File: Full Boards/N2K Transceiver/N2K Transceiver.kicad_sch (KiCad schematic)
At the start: 67 parts, among them J1 PSU TP, J3 Optional Bond, SW1 SW_MEC_5G, SW2 SW_MEC_5G, SW3 SW_MEC_5G

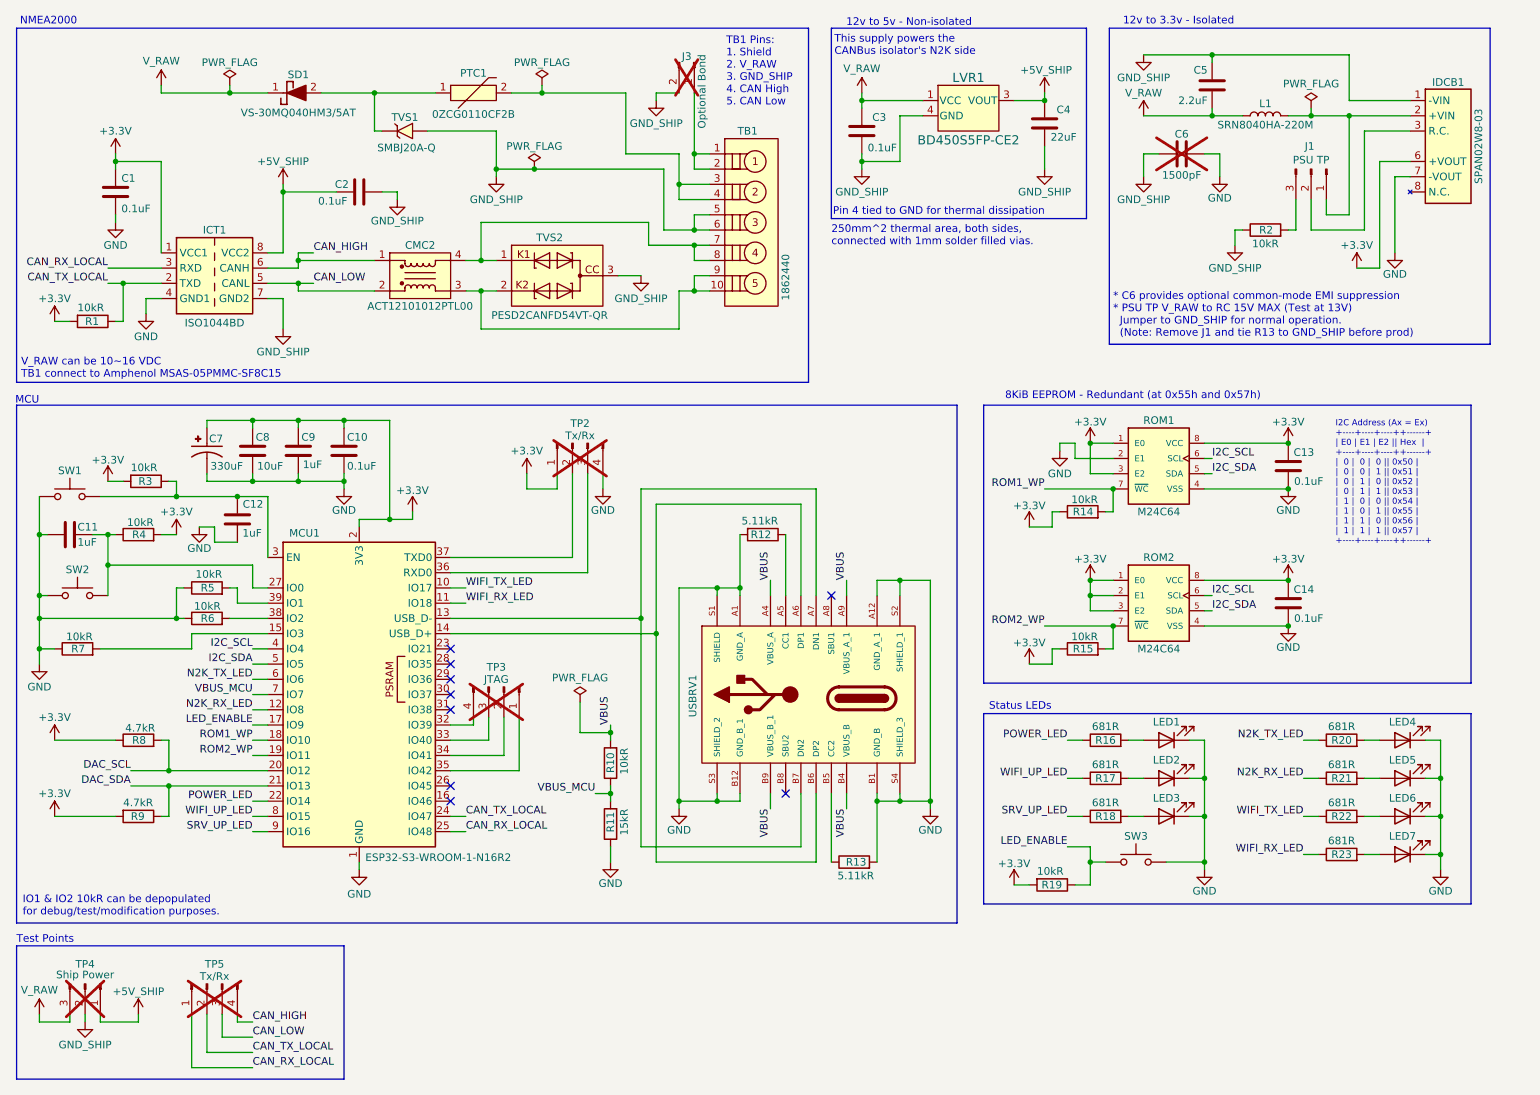
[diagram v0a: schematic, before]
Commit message: Added pull-ups to the I2C SDA/SCL pins. Removed old DAC pull-ups and nets. Added a space between the CAN-H/L and Tx/Rx test points for isolation.
Signed-off-by: digimer <digital.mermaid@gmail.com>
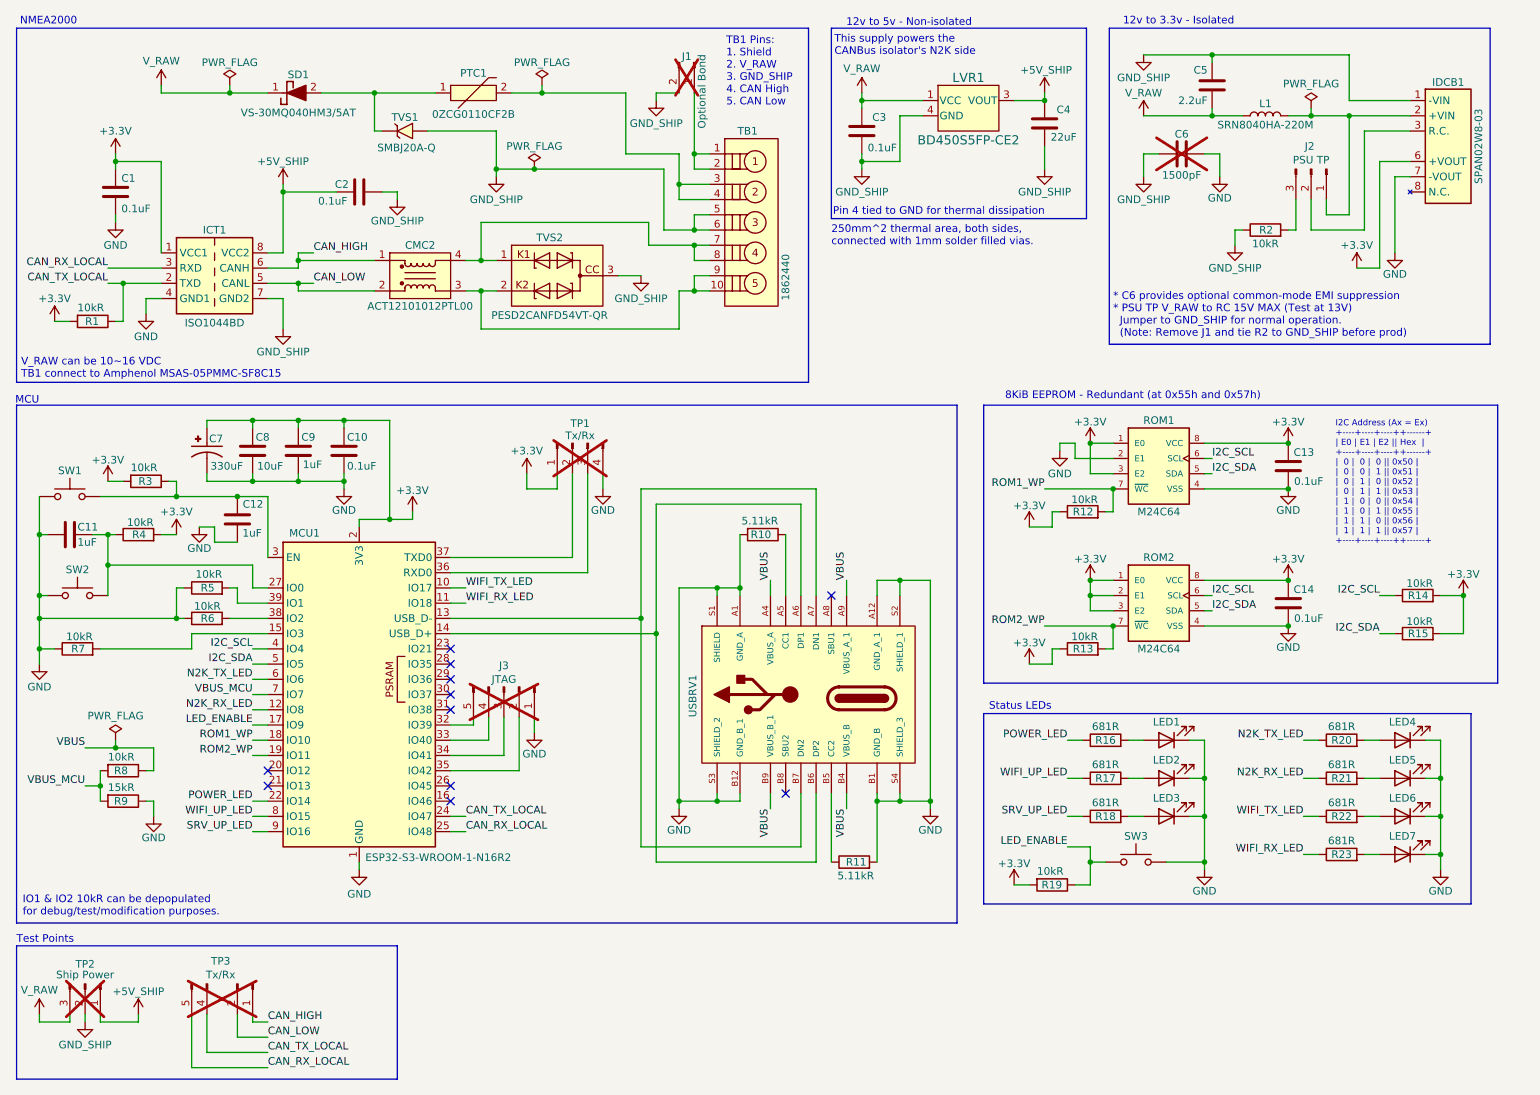
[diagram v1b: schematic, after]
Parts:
- removed R8, R9: 4.7kR, mr-stuff:Stackpole_RNCP1206, symbol Device:R
- removed TP5: Tx/Rx, Connector_PinHeader_2.54mm:PinHeader_1x04_P2.54mm_Vertical, symbol Connector:Conn_01x04_Pin
- added R14, R15: 10kR, mr-stuff:Stackpole_RNCP1206, symbol Device:R
- added TP3: Tx/Rx, symbol mr-parts:Conn_01x05_Pin_No_Pin_3
- J3: renamed from TP3; footprint Connector_PinHeader_2.54mm:PinHeader_1x04_P2.54mm_Vertical -> Connector_PinHeader_2.54mm:PinHeader_1x05_P2.54mm_Vertical; symbol Connector:Conn_01x04_Pin -> Connector:Conn_01x05_Pin; Part Amphenol 68001-416HLF -> (none); now in the parts list
- renumbered J3 to J1, J1 to J2, R12 to R10, R13 to R11, R14 to R12, R15 to R13, R10 to R8, R11 to R9, TP2 to TP1, TP4 to TP2
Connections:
- net +3.3V: now also R14.2, R15.2
- net CAN_HIGH: now also TP3.1 (Pin_1)
- net CAN_LOW: now also TP3.2 (Pin_2)
- net CAN_RX_LOCAL: now also TP3.5 (Pin_5)
- net CAN_TX_LOCAL: now also TP3.4 (Pin_4)
- net GND: now also J3.1 (Pin_1)
- net I2C_SCL: now also R14.1
- net I2C_SDA: now also R15.1
- net VBUS: now also R8.1; no longer R8.2
- net VBUS_MCU: now also R8.2; no longer R8.1
- net at MCU1.35 (IO42): now also J3.2 (Pin_2); no longer J3.1 (Pin_1)
- net at MCU1.34 (IO41): now also J3.3 (Pin_3); no longer J3.2 (Pin_2)
- net at MCU1.33 (IO40): now also J3.4 (Pin_4); no longer J3.3 (Pin_3)
- net at MCU1.32 (IO39): now also J3.5 (Pin_5); no longer J3.4 (Pin_4)
- net DAC_SCL: no longer names the net of MCU1.20 (IO12)
- net DAC_SDA: no longer names the net of MCU1.21 (IO13)
- no-connect marks 9 -> 11
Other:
- note added: "* C6 provides optional common-mode EMI suppression * PSU TP V_RAW to RC 15V MAX (Test at 13V) Jumper to GND_SHIP for normal operation. (Note: Remove J1 and tie R2 to GND_SHIP before prod)"
- note removed: "* C6 provides optional common-mode EMI suppression * PSU TP V_RAW to RC 15V MAX (Test at 13V) Jumper to GND_SHIP for normal operation. (Note: Remove J1 and tie R13 to GND_SHIP before prod)"
- moved on the sheet: R8, R9

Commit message: Initial PCB layout complete.
Signed-off-by: digimer <digital.mermaid@gmail.com>
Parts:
- added FID1, FID2, FID3: Fiducial, Fiducial:Fiducial_1mm_Mask2mm, symbol Mechanical:Fiducial
- added H1, H2, H3, H4: MountingHole_Pad, MountingHole:MountingHole_4mm_Pad_Via, symbol Mechanical:MountingHole_Pad
- J2: footprint (none) -> Connector_PinHeader_2.54mm:PinHeader_1x03_P2.54mm_Vertical
- TP1: value Tx/Rx -> MCU Tx/Rx
- TP3: value Tx/Rx -> CAN Tx/Rx; footprint (none) -> mr-stuff:PinHeader_1x05_P2.54mm_Vertical_No_Pin_3
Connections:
- net GND_SHIP: now also H1.1, H2.1, H3.1, H4.1
- net N2K_RX_LED: now also R23.1; no longer R21.1
- net N2K_TX_LED: now also R22.1; no longer R20.1
- net WIFI_RX_LED: now also R21.1; no longer R23.1
- net WIFI_TX_LED: now also R20.1; no longer R22.1
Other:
- note added: "Boot"
- note added: "Mounts and Fiducials"
- note added: "Reset"

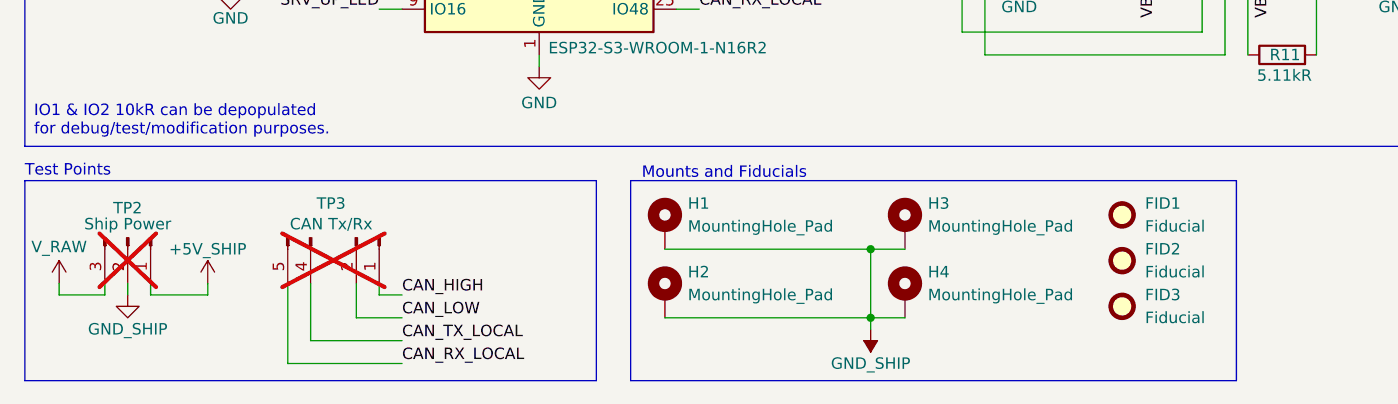
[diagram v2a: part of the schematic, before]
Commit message: Unlinked mounting holes from ship's ground.
Signed-off-by: digimer <digital.mermaid@gmail.com>
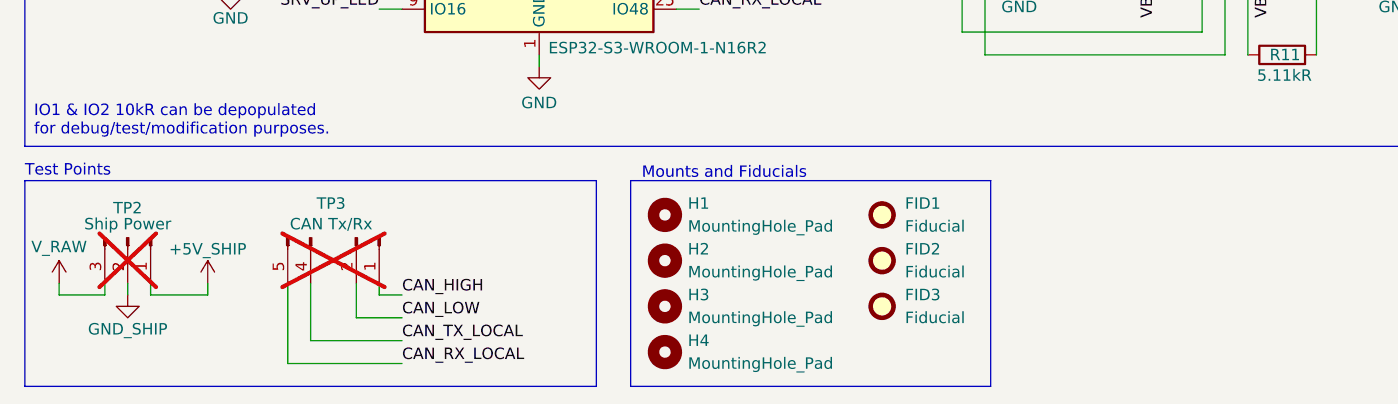
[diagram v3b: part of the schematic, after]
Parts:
- H1, H2, H3, H4: footprint MountingHole:MountingHole_4mm_Pad_Via -> MountingHole:MountingHole_4.3mm_M4_Pad; symbol Mechanical:MountingHole_Pad -> Mechanical:MountingHole
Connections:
- net GND_SHIP: no longer H1.1, H2.1, H3.1, H4.1
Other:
- moved on the sheet: FID1, FID2, FID3

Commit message: Made mounting holes unplated.
Signed-off-by: digimer <digital.mermaid@gmail.com>
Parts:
- H1, H2, H3, H4: footprint MountingHole:MountingHole_4.3mm_M4_Pad -> MountingHole:MountingHole_4.3mm_M4
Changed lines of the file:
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@@
 			)
 		)
-		(property "Footprint" "MountingHole:MountingHole_4.3mm_M4_Pad"
+		(property "Footprint" "MountingHole:MountingHole_4.3mm_M4"
 			(at 86.36 182.88 0)
 			(hide yes)
@@
 			)
 		)
-		(property "Footprint" "MountingHole:MountingHole_4.3mm_M4_Pad"
+		(property "Footprint" "MountingHole:MountingHole_4.3mm_M4"
 			(at 86.36 187.96 0)
 			(hide yes)
@@
 			)
 		)
-		(property "Footprint" "MountingHole:MountingHole_4.3mm_M4_Pad"
+		(property "Footprint" "MountingHole:MountingHole_4.3mm_M4"
 			(at 86.36 172.72 0)
 			(hide yes)
@@
 			)
 		)
-		(property "Footprint" "MountingHole:MountingHole_4.3mm_M4_Pad"
+		(property "Footprint" "MountingHole:MountingHole_4.3mm_M4"
 			(at 86.36 177.8 0)
 			(hide yes)

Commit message: Added supply-side caps and permantently connected the R.C. pull-down resistor.
Signed-off-by: digimer <digital.mermaid@gmail.com>
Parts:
- added C7: 0.1uF, mr-stuff:Kyocera AVX 0805, symbol Device:C
- added C8: 10uF, mr-stuff:TDK CGA5, symbol Device:C
- J2: footprint Connector_PinHeader_2.54mm:PinHeader_1x03_P2.54mm_Vertical -> Connector_PinHeader_2.54mm:PinHeader_1x02_P2.54mm_Vertical; symbol Connector:Conn_01x03_Pin -> Connector:Conn_01x02_Pin
- renumbered C8 to C10, C9 to C11, C10 to C12, C11 to C13, C12 to C14, C13 to C15, C14 to C16, C7 to C9
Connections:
- net +3.3V: now also C7.1, C8.2
- net GND: now also C7.2, C8.1
- net at IDCB1.3 (R.C.), J2.2 (Pin_2): now also R2.2
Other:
- moved on the sheet: R2

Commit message: Reworked the CAN TVS/CMC to help balance lead length.
Signed-off-by: digimer <digital.mermaid@gmail.com>
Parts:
- renumbered CMC2 to CMC1
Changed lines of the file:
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@@
 		(in_pos_files yes)
 		(dnp no)
-		(property "Reference" "CMC2"
+		(property "Reference" "CMC1"
 			(at 82.55 52.07 0)
 			(show_name no)
@@
 			(project "N2K Transceiver"
 				(path "/2a070473-cb6e-4844-8f2a-5ea6a35ddb49"
-					(reference "CMC2")
+					(reference "CMC1")
 					(unit 1)
 				)
